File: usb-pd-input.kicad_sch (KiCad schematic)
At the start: 23 parts, among them J1 USB-C, J2 Pogo pads, J3 Pogo pads (debug), Q1 -30V -4A, U1 STUSB4500QTR

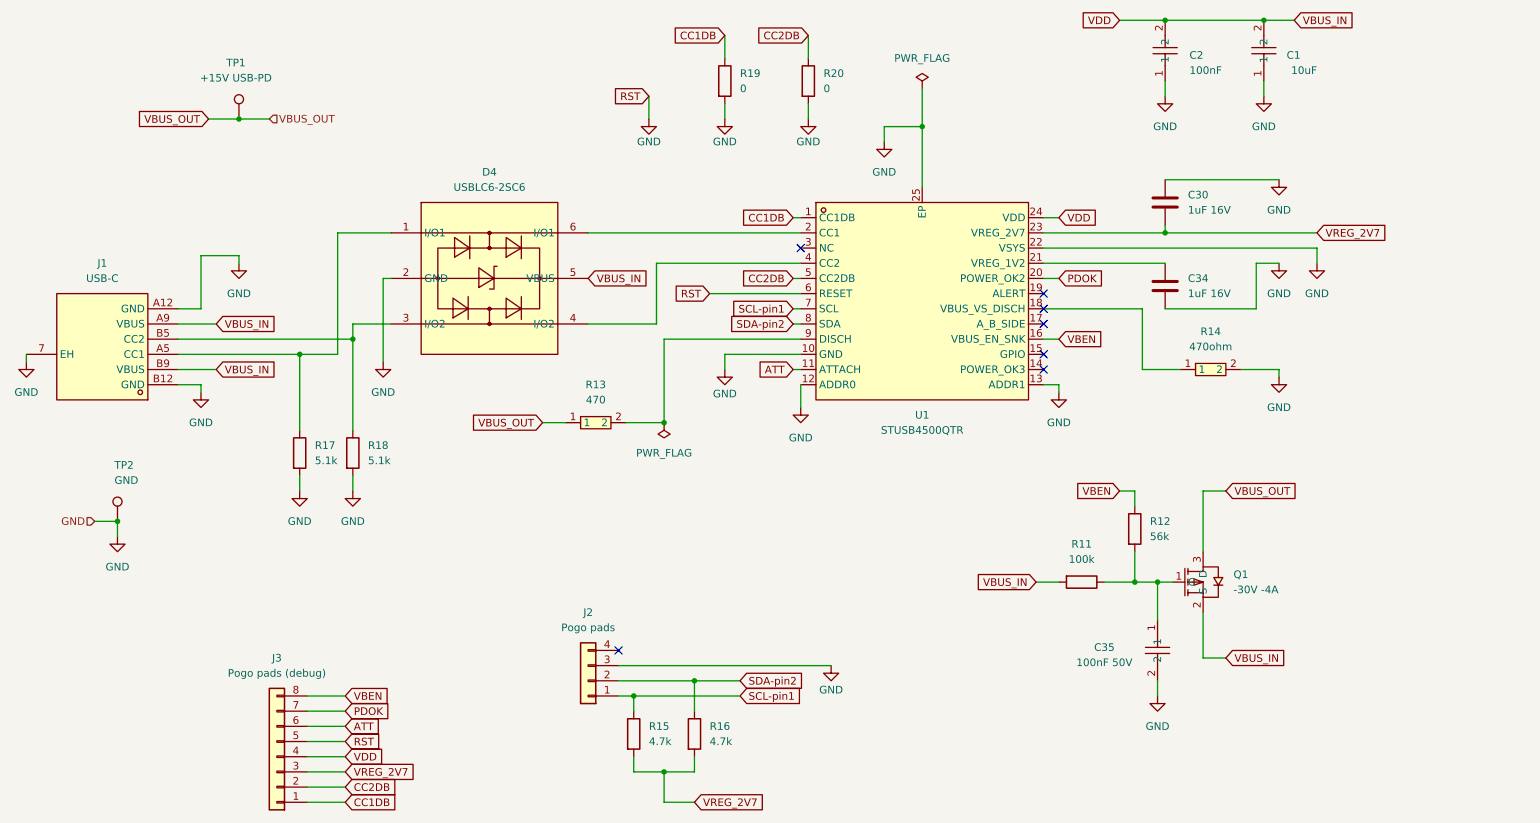
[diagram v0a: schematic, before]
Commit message: fix(usb-pd): wire STUSB4500 pin18 VBUS_VS_DISCH to VBUS_IN via R14 series resistor
This fixes the root cause of v3 failing to negotiate USB-PD. Pin 18
(VBUS_VS_DISCH) was left floating. Corrections:
- Wire pin 18 to VBUS_IN through series resistor R14 (470Ω)
- Add test point TP6 on VBUS_VS_DISCH net for diagnostics
- Fix R14 footprint from unresolved easyeda2kicad:R0603 to zudo-pd:R0603
- Remove incorrect divider-to-GND resistor network (now single series topology)
- Update PCB layout to match schematic changes (R14 placement, TP6, routing)

Co-Authored-By: Claude Opus 4.8 (1M context) <noreply@anthropic.com>
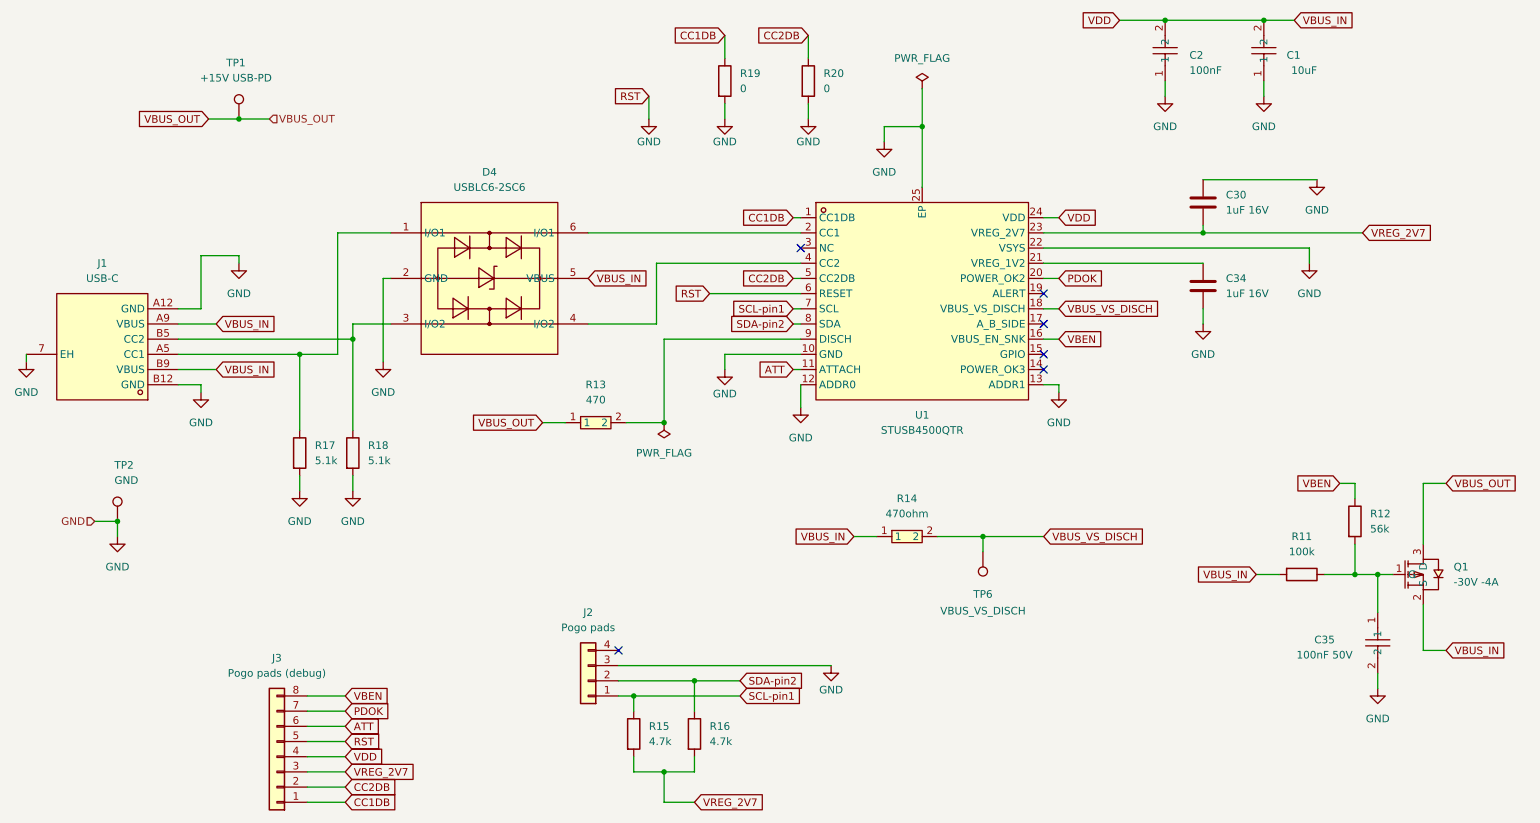
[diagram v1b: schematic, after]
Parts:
- added TP6: VBUS_VS_DISCH, TestPoint:TestPoint_Pad_D1.5mm, symbol Connector:TestPoint
- R14: footprint easyeda2kicad:R0603 -> zudo-pd:R0603
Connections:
- net GND: no longer R14.2
- net VBUS_IN: now also R14.1
- net VBUS_VS_DISCH: now reaches U1.18 (VBUS_VS_DISCH)
- net VBUS_VS_DISCH: now also R14.2, TP6.1; no longer R14.1
- no-connect marks 7 -> 6
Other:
- moved on the sheet: C30, C34, C35, Q1, R11, R12

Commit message: fix(usb-pd): v0.4.0 faston swap to C591344 + harmonize BOM comments
- J6-J9 faston: C305825 (TE 1217754-1, out of stock) -> C591344
  (TE 63951-1, same physical tab/footprint, strip packaging)
- Harmonize Comment/Value so duplicate-LCSC lines collapse to one
  BOM row each: 470ohm (R13,R14), 100nF 50V (8x), 470uF 16V (C4,C22,C23)
- PCB synced from schematic (Update PCB from Schematic)

Co-Authored-By: Claude Opus 4.8 (1M context) <noreply@anthropic.com>
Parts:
- C2: value 100nF -> 100nF 50V
- R13: value 470 -> 470ohm
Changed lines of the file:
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@@
 			)
 		)
-		(property "Value" "470"
+		(property "Value" "470ohm"
 			(at 121.92 80.01 0)
 			(show_name no)
@@
 			)
 		)
-		(property "Value" "100nF"
+		(property "Value" "100nF 50V"
 			(at 221.234 24.892 90)
 			(show_name no)
